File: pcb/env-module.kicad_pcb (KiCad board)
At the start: 4 copper layers, 50 x 30 mm, 68 parts, among them J10 Power Out, J2 QWICC, J5 QWICC, J7 Power In, J9 AVR-UPDI-6, U1 ATtiny1616-MNR, U2 HDC1080, U3 LTR-303ALS-01

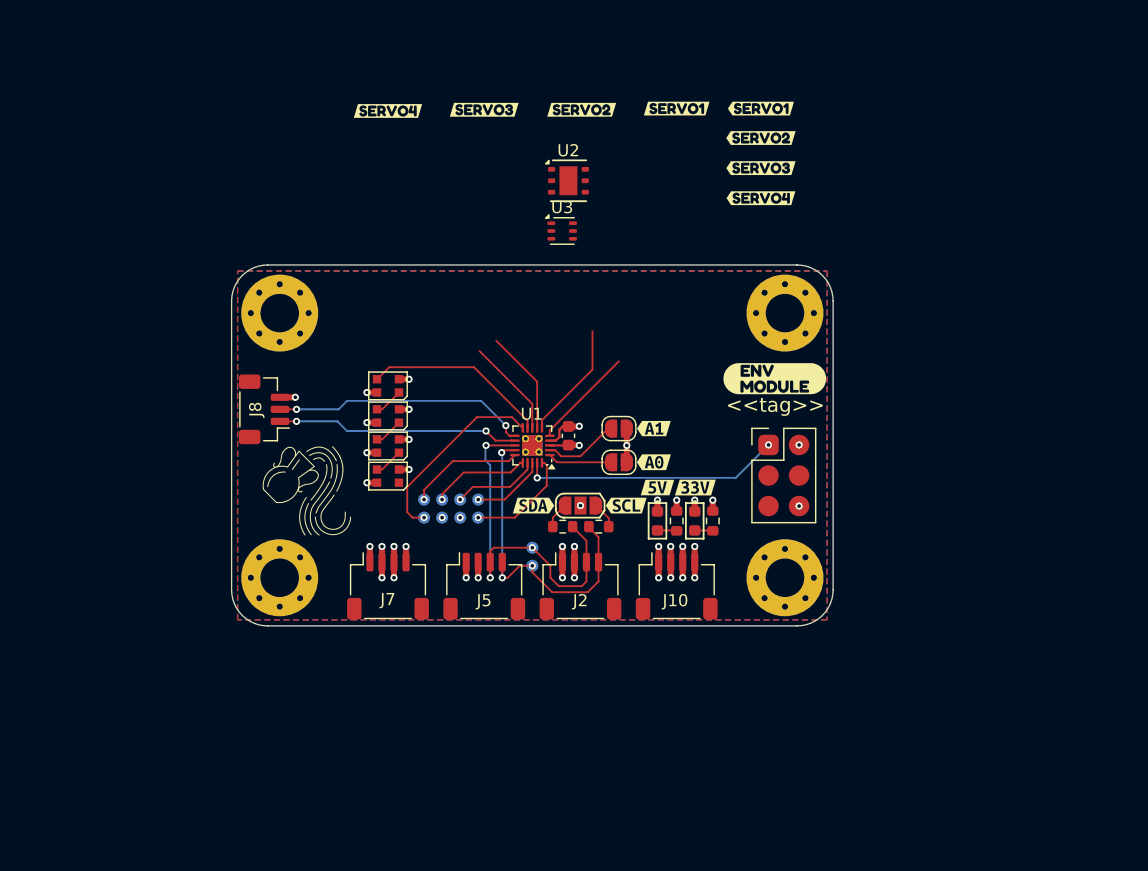
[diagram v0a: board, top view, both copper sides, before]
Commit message: Updated license and implemented RP2040
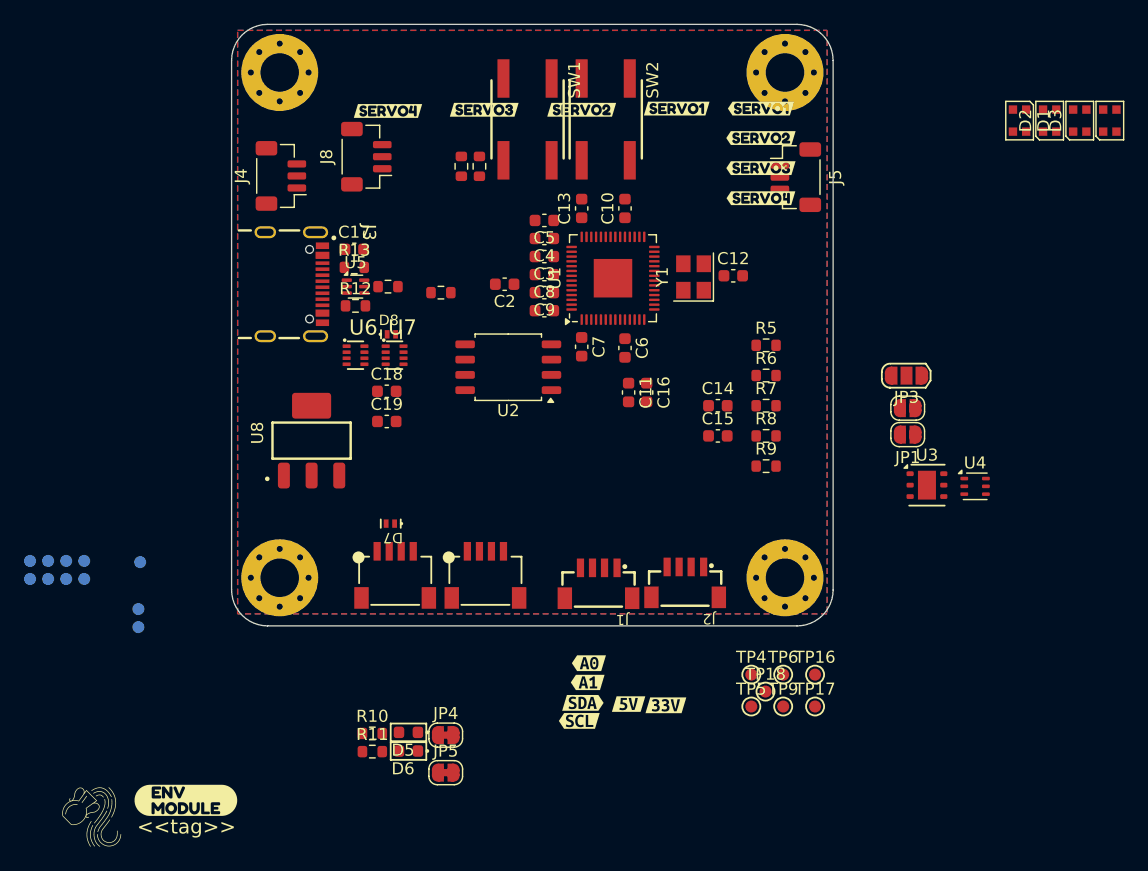
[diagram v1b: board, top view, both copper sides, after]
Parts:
- removed J10: Power Out, CRGM Connector:JST_SH_SM04B-SRSS-TB_1x04-1MP_P1.00mm_Horizontal
- removed J9: AVR-UPDI-6, CRGM Connector:PinHeader_2x03_P2.54mm_Vertical_SMD
- added C10: 0.1uF, Capacitor_SMD:C_0603_1608Metric, F.Cu at (82.7, 75.3)
- added C11: 0.1uF, Capacitor_SMD:C_0603_1608Metric, F.Cu at (83.0, 90.6)
- added C12: 0.1uF, Capacitor_SMD:C_0603_1608Metric, F.Cu at (91.7, 80.9)
- added C13: 0.1uF, Capacitor_SMD:C_0603_1608Metric, F.Cu at (79.1, 75.3)
- added C14: 15pF, Capacitor_SMD:C_0603_1608Metric, F.Cu at (90.4, 91.7)
- added C15: 15pF, Capacitor_SMD:C_0603_1608Metric, F.Cu at (90.4, 94.2)
- added C16: 10uF, Capacitor_SMD:C_0603_1608Metric, F.Cu at (84.5, 90.6)
- added C17: 0.1uF, Capacitor_SMD:C_0603_1608Metric, F.Cu at (60.2, 78.7)
- added C18: 0.1uF, Capacitor_SMD:C_0603_1608Metric, F.Cu at (62.9, 90.5)
- added C19: 10uF, Capacitor_SMD:C_0603_1608Metric, F.Cu at (62.9, 93.0)
- added C2: 0.1uF, Capacitor_SMD:C_0603_1608Metric, F.Cu at (72.7, 81.6)
- added C3: 1uF, Capacitor_SMD:C_0603_1608Metric, F.Cu at (76.0, 79.3)
- added C4: 1uF, Capacitor_SMD:C_0603_1608Metric, F.Cu at (76.0, 77.8)
- added C5: 0.1uF, Capacitor_SMD:C_0603_1608Metric, F.Cu at (76.0, 76.3)
- added C6: 0.1uF, Capacitor_SMD:C_0603_1608Metric, F.Cu at (82.7, 86.9)
- added C7: 0.1uF, Capacitor_SMD:C_0603_1608Metric, F.Cu at (79.1, 86.8)
- added C8: 0.1uF, Capacitor_SMD:C_0603_1608Metric, F.Cu at (76.0, 80.8)
- added C9: 0.1uF, Capacitor_SMD:C_0603_1608Metric, F.Cu at (76.0, 82.3)
- added D1: WS2812B-2020, LED_SMD:LED_WS2812B-2020_PLCC4_2.0x2.0mm, F.Cu at (115.5, 68.0)
- added D8: PESD3V3S1BL, CRGM Passive:DFN1006-2, F.Cu at (63.3, 85.8)
- added J1: ~, CRGM Connector:BM04B-SRSS-TB, F.Cu at (80.5, 105.2)
- added J3: USB_C_USB2.0_16P, CRGM Connector:GCT_USB4105-GF-A, F.Cu at (52.8, 81.6)
- added J4: ~, Connector_JST:JST_SH_BM03B-SRSS-TB_1x03-1MP_P1.00mm_Vertical, F.Cu at (54.1, 72.6)
- added J6: ~, CRGM Connector:SM04B-SRSS-TB, F.Cu at (71.1, 103.8)
- added JP4: ~, CRGM Connector:SolderJumper-2_P1.3mm_Bridged_RoundedPad1.0x1.5mm, F.Cu at (67.8, 119.1)
- added JP5: ~, CRGM Connector:SolderJumper-2_P1.3mm_Bridged_RoundedPad1.0x1.5mm, F.Cu at (67.8, 122.2)
- added R10: 4.7K, Resistor_SMD:R_0603_1608Metric, F.Cu at (61.7, 118.9)
- added R11: 1K, Resistor_SMD:R_0603_1608Metric, F.Cu at (61.7, 120.5)
- added R12: 5.1K, Resistor_SMD:R_0603_1608Metric, F.Cu at (60.3, 83.4)
- added R13: 5.1K, Resistor_SMD:R_0603_1608Metric, F.Cu at (60.2, 80.2)
- added R5: 4.7K, Resistor_SMD:R_0603_1608Metric, F.Cu at (94.4, 86.7)
- added R6: 4.7K, Resistor_SMD:R_0603_1608Metric, F.Cu at (94.4, 89.2)
- added R7: 1K, Resistor_SMD:R_0603_1608Metric, F.Cu at (94.4, 91.7)
- added R8: 4.7K, Resistor_SMD:R_0603_1608Metric, F.Cu at (94.4, 94.2)
- added R9: 4.7K, Resistor_SMD:R_0603_1608Metric, F.Cu at (94.4, 96.7)
- added SW1: EVQ-Q2B02W, CRGM Switches:EVQ-Q2B02W, F.Cu at (74.6, 67.9)
- added SW2: EVQ-Q2B02W, CRGM Switches:EVQ-Q2B02W, F.Cu at (81.1, 67.9)
- added TP16: ~, CRGM Mechanical:TestPoint_Pad_D1.0mm, F.Cu at (98.5, 114.0)
- added TP17: ~, CRGM Mechanical:TestPoint_Pad_D1.0mm, F.Cu at (98.5, 116.7)
- added TP18: ~, CRGM Mechanical:TestPoint_Pad_D1.0mm, F.Cu at (94.4, 115.5)
- added TP4: ~, CRGM Mechanical:TestPoint_Pad_D1.0mm, F.Cu at (93.2, 114.0)
- added TP5: ~, CRGM Mechanical:TestPoint_Pad_D1.0mm, F.Cu at (93.2, 116.7)
- added TP6: ~, CRGM Mechanical:TestPoint_Pad_D1.0mm, F.Cu at (95.8, 114.0)
- added TP9: ~, CRGM Mechanical:TestPoint_Pad_D1.0mm, F.Cu at (95.8, 116.7)
- added U4: LTR-303ALS-01, CRG Makes:LTR-303ALS-01, F.Cu at (111.8, 98.4)
- added U5: USBLC6-2P6, Package_TO_SOT_SMD:SOT-666, F.Cu at (60.3, 81.8)
- added U6: LM66200DRLR, CRGM Power:SOTFL50P160X60-8N, F.Cu at (60.3, 87.5)
- added U7: LM66200DRLR, CRGM Power:SOTFL50P160X60-8N, F.Cu at (63.5, 87.5)
- added U8: LD1117S33TR, CRGM Power:SOT230P700X180-4N, F.Cu at (56.6, 94.6)
- added Y1: ABM8-272-T3, CRGM Passive:Crystal_SMD_3225-4Pin_3.2x2.5mm, F.Cu at (88.4, 81.0)
- D2: value Orange -> WS2812B-2020; footprint LED_SMD:LED_0603_1608Metric -> LED_SMD:LED_WS2812B-2020_PLCC4_2.0x2.0mm
- D3: value Blue -> WS2812B-2020; footprint LED_SMD:LED_0603_1608Metric -> LED_SMD:LED_WS2812B-2020_PLCC4_2.0x2.0mm
- D5, D6: value WS2812B-2020 -> Orange; footprint LED_SMD:LED_WS2812B-2020_PLCC4_2.0x2.0mm -> LED_SMD:LED_0603_1608Metric
- D7: value WS2812B-2020 -> PESD5V5C1BL; footprint LED_SMD:LED_WS2812B-2020_PLCC4_2.0x2.0mm -> CRGM Passive:DFN1006-2
- J2: value QWICC -> ~; footprint CRGM Connector:JST_SH_SM04B-SRSS-TB_1x04-1MP_P1.00mm_Horizontal -> CRGM Connector:BM04B-SRSS-TB
- J5: value QWICC -> ~; footprint CRGM Connector:JST_SH_SM04B-SRSS-TB_1x04-1MP_P1.00mm_Horizontal -> Connector_JST:JST_SH_BM03B-SRSS-TB_1x03-1MP_P1.00mm_Vertical
- J7: value Power In -> ~; footprint CRGM Connector:JST_SH_SM04B-SRSS-TB_1x04-1MP_P1.00mm_Horizontal -> CRGM Connector:SM04B-SRSS-TB
- J8: value ~ -> BM03B-SRSS-TB; footprint CRGM Connector:JST_SH_BM03B-SRSS-TB_1x03-1MP_P1.00mm_Vertical -> Connector_JST:JST_SH_BM03B-SRSS-TB_1x03-1MP_P1.00mm_Vertical
- JP1: value Jumper_3_Open -> ~; footprint CRGM Connector:SolderJumper-3_P1.3mm_Open_RoundedPad1.0x1.5mm -> CRGM Connector:SolderJumper-2_P1.3mm_Open_RoundedPad1.0x1.5mm
- JP2: value A0 -> ~
- JP3: value A1 -> Jumper_3_Open; footprint CRGM Connector:SolderJumper-2_P1.3mm_Open_RoundedPad1.0x1.5mm -> CRGM Connector:SolderJumper-3_P1.3mm_Open_RoundedPad1.0x1.5mm
- LOGO1: footprint CRGM Logos:Aquarius Logo 8mm -> CRGM Logos:CRGM Logo 10mm
- LOGO2: footprint CRGM Logos:Aquarius Logo 8mm -> CRGM Logos:Aquarius Logo 5mm
- LOGO3: value Logo_Open_Hardware_Small -> ~; footprint Symbol:OSHW-Logo_5.7x6mm_SilkScreen -> CRGM Logos:Aquarius Logo 5mm
- LOGO4: value ~ -> Logo_Open_Hardware_Small; footprint CRGM Logos:CRGM Logo 5mm -> Symbol:OSHW-Logo_5.7x6mm_SilkScreen
- R1: value 4.7K -> 10K
- R2: value 4.7K -> 1K
- R3: value 4.7K -> 27
- R4: value 1K -> 27
- TP1: value PA1 -> ~
- TP10: value UPDI -> ~
- TP11: value V33 -> ~
- TP12: value GND -> ~
- TP13: value PB3 -> ~
- TP14: value PC3 -> ~
- TP15: value PC2 -> ~
- TP2: value PC0 -> ~
- TP3: value PC1 -> ~
- TP7: value SCL -> ~
- TP8: value SDA -> ~
- U1: value ATtiny1616-MNR -> RP2040; footprint CRG Makes:VQFN-20-1EP_3x3mm_P0.4mm_EP1.7x1.7mm_ThermalVias -> Package_DFN_QFN:QFN-56-1EP_7x7mm_P0.4mm_EP3.2x3.2mm
- U2: value HDC1080 -> W25Q128JVS; footprint CRG Makes:PWSON-N6 -> CRG Makes:SOIC-8_5.3x5.3mm_P1.27mm
- U3: value LTR-303ALS-01 -> HDC1080; footprint CRG Makes:LTR-303ALS-01 -> CRG Makes:PWSON-N6
- moved D4 63.9 mm to (123.0, 68.0), turned to 90 degrees
- moved kibuzzard-68645E77 60.2 mm to (46.2, 124.5)
- moved TP10 53.1 mm to (42.4, 104.7)
- moved D2 46.6 mm to (118.0, 68.0), turned to 90 degrees
- moved D3 46.2 mm to (120.5, 68.0), turned to 90 degrees
- moved J5 42.7 mm to (96.9, 72.7), turned to -90 degrees
- moved LOGO1 42.7 mm to (82.4, 132.3)
- moved kibuzzard-68586251 42.6 mm to (25.8, 111.0)
- moved kibuzzard-6861B7EA 42.6 mm to (28.8, 111.0)
- moved kibuzzard-6861B80B 42.6 mm to (30.2, 111.0)
- moved kibuzzard-6861B833 42.6 mm to (27.3, 111.0)
- moved kibuzzard-68645E60 42.2 mm to (63.5, 126.0)
- moved kibuzzard-6861B880 41.9 mm to (27.2, 114.9)
- moved kibuzzard-6861B899 41.9 mm to (25.7, 114.9)
- moved kibuzzard-6862CEAB 41.9 mm to (30.2, 114.9)
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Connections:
- net SERVO1 renamed MOSI
- net SERVO2 renamed MISO
- net SERVO4 renamed SCK
- C1 pad 1: +3.3V -> +1V1
- D2 pad 1: GND -> Net-(D2-DOUT)
- D2 pad 2: /Indicators/V5LED -> GND
- D3 pad 1: GND -> Net-(D3-DOUT)
- D3 pad 2: /Indicators/V3.3LED -> GND
- D4 pad 1: Net-(D4-DOUT) -> unconnected-(D4-DOUT-Pad1)
- D4 pad 3: STATUS_LEDS -> Net-(D3-DOUT)
- D5 pad 1: Net-(D5-DOUT) -> Net-(D5-K)
- D5 pad 2: GND -> /Indicators/V5LED
- D6 pad 1: Net-(D6-DOUT) -> Net-(D6-K)
- D6 pad 2: GND -> /Indicators/V3.3LED
- D7 pad 1: unconnected-(D7-DOUT-Pad1) -> GND
- D7 pad 2: GND -> LINE_5V
- J2 pad 3: SDA -> SDA_EXT
- J2 pad 4: SCL -> SCL_EXT
- J5 pad 1: GND -> SWCLK
- J5 pad 2: +3.3V -> GND
- J5 pad 3: SDA -> SWD
- J7 pad 1: +5V -> LINE_5V
- J7 pad 4: +3.3V -> LINE_V33
- J8 pad 1: TXD -> GND
- J8 pad 2: RXD -> +3.3V
- J8 pad 3: GND -> EXT_LEDS
- JP1 pad 1: Net-(JP1-A) -> GND
- JP1 pad 2: +3.3V -> /MCU/A1
- JP3 pad 1: GND -> Net-(JP3-A)
- JP3 pad 2: /MCU/A1 -> +3.3V
- R1 pad 1: SDA -> +3.3V
- R1 pad 2: Net-(JP1-B) -> /MCU/QSPI_CS
- R2 pad 1: SCL -> USBBOOT
- R2 pad 2: Net-(JP1-A) -> /MCU/QSPI_CS
- R3 pad 1: +5V -> Net-(U1-USB_DP)
- R3 pad 2: /Indicators/V5LED -> D_P
- R4 pad 1: +3.3V -> Net-(U1-USB_DM)
- R4 pad 2: /Indicators/V3.3LED -> D_N
- TP1 pad 1: /MCU/PA1 -> USB_5V
- TP10 pad 1: UPDI -> SWCLK
- TP11 pad 1: +3.3V -> SWD
- TP12 pad 1: GND -> LINE_V33
- TP13 pad 1: /MCU/PB4 -> LINE_5V
- TP14 pad 1: /MCU/PC3 -> EXT_LEDS
- TP15 pad 1: /MCU/PC2 -> +5V
- TP2 pad 1: /MCU/PC0 -> SCL_EXT
- TP3 pad 1: /MCU/PC1 -> SDA_EXT
- TP7 pad 1: SCL -> D_P
- TP8 pad 1: SDA -> TXD
- U1 pad 1: /MCU/A0 -> +3.3V
- U1 pad 10: /MCU/PB4 -> +3.3V
- U1 pad 11: RXD -> EXT_LEDS
- U1 pad 12: TXD -> unconnected-(U1-GPIO9-Pad12)
- U1 pad 13: SDA -> unconnected-(U1-GPIO10-Pad13)
- U1 pad 14: SCL -> unconnected-(U1-GPIO11-Pad14)
- U1 pad 15: /MCU/PC0 -> unconnected-(U1-GPIO12-Pad15)
- U1 pad 16: /MCU/PC1 -> unconnected-(U1-GPIO13-Pad16)
- U1 pad 17: /MCU/PC2 -> unconnected-(U1-GPIO14-Pad17)
- U1 pad 18: /MCU/PC3 -> unconnected-(U1-GPIO15-Pad18)
- U1 pad 19: UPDI -> GND
- U1 pad 2: /MCU/A1 -> /MCU/A0
- U1 pad 20: /MCU/PA1 -> Net-(U1-XIN)
- U1 pad 21: GND -> Net-(U1-XOUT)
- U1 pad 3: GND -> /MCU/A1
- U1 pad 4: +3.3V -> unconnected-(U1-GPIO2-Pad4)
- U1 pad 7: SERVO3 -> RXD
- U1 pad 9: STATUS_LEDS -> OBLEDS
- U2 pad 1: unconnected-(U2-SDA-Pad1) -> /MCU/QSPI_CS
- U2 pad 2: unconnected-(U2-GND-Pad2) -> /MCU/QSPI_D1
- U2 pad 3: unconnected-(U2-NC-Pad3) -> /MCU/QSPI_D2
- U2 pad 4: unconnected-(U2-NC-Pad4) -> GND
- U2 pad 5: unconnected-(U2-VCC-Pad5) -> /MCU/QSPI_D0
- U2 pad 6: unconnected-(U2-SCL-Pad6) -> /MCU/QSPI_SCK
- U2 pad 7: unconnected-(U2-DAP-Pad7) -> /MCU/QSPI_D3
- U3 pad 1: unconnected-(U3-VDD-Pad1) -> SDA_INT
- U3 pad 2: unconnected-(U3-NC-Pad2) -> GND
- U3 pad 5: unconnected-(U3-INT-Pad5) -> +3.3V
- U3 pad 6: unconnected-(U3-SDA-Pad6) -> SCL_INT
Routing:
- net SDA: track 31.0 -> 0.00 mm, vias 3 -> 0
- net SCL: track 27.8 -> 0.00 mm, vias 3 -> 0
- net GND: track 26.1 -> 0.00 mm, vias 22 -> 0
- net UPDI: track 21.6 -> 0.00 mm, vias 2 -> 0
- net RXD: track 21.3 -> 0.00 mm, vias 2 -> 0
- net TXD: track 20.2 -> 0.00 mm, vias 2 -> 0
- net /MCU/PB4: track 16.3 -> 0.00 mm, vias 1 -> 0
- net STATUS_LEDS: track 15.4 -> 0.00 mm
- net +3.3V: track 15.3 -> 0.00 mm, vias 15 -> 0
- net MISO: track 9.79 -> 0.00 mm
- net /MCU/PC0: track 9.55 -> 0.00 mm, vias 1 -> 0
- net /MCU/PA1: track 8.98 -> 0.00 mm, vias 1 -> 0
- net SERVO3: track 8.66 -> 0.00 mm
- net MOSI: track 8.58 -> 0.00 mm
- net /MCU/PC1: track 8.23 -> 0.00 mm, vias 1 -> 0
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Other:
- board size 50 x 30 mm -> 50 x 50 mm

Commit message: Added interfaces and fully routed PCB
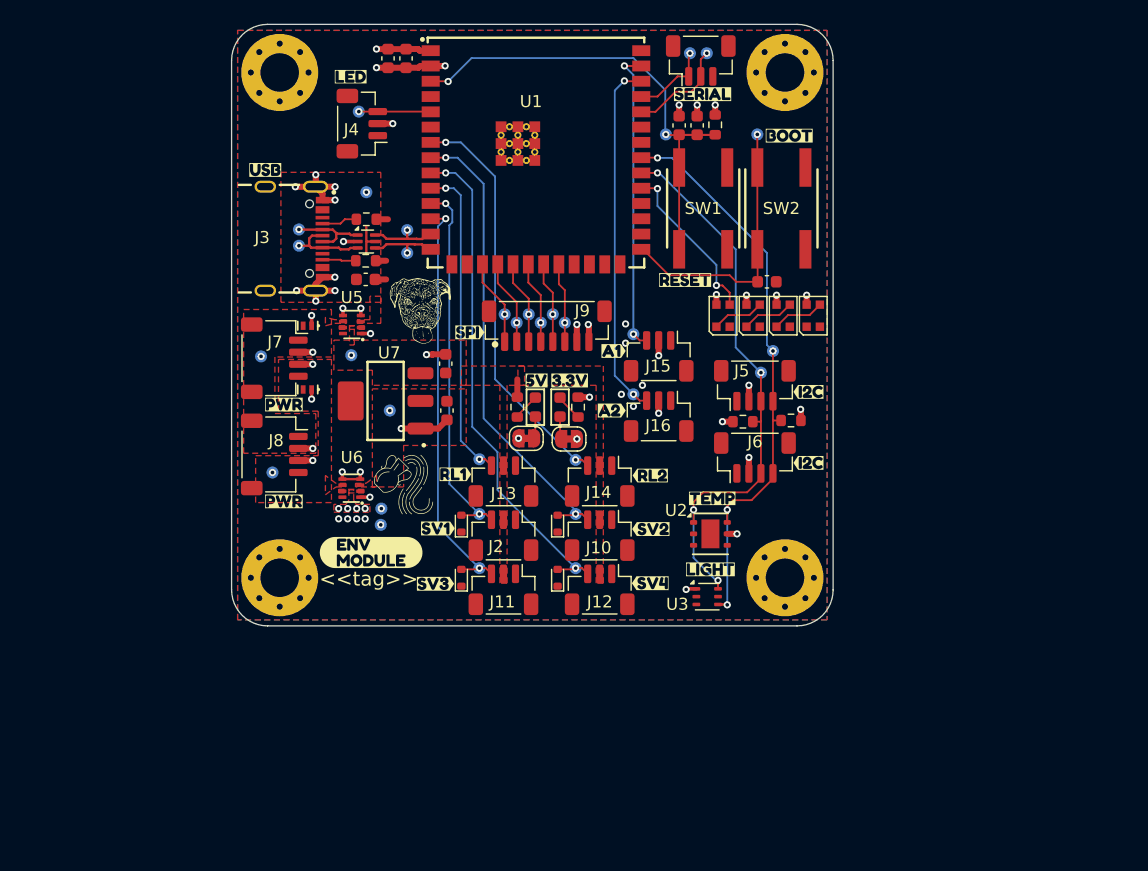
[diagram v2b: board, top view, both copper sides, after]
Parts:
- removed C10, C11, C12, C13, C17, C18, C9: 0.1uF, Capacitor_SMD:C_0603_1608Metric
- removed C14, C15: 15pF, Capacitor_SMD:C_0603_1608Metric
- removed C16, C19: 10uF, Capacitor_SMD:C_0603_1608Metric
- removed JP1: ~, CRGM Connector:SolderJumper-2_P1.3mm_Open_RoundedPad1.0x1.5mm
- removed JP4, JP5: ~, CRGM Connector:SolderJumper-2_P1.3mm_Bridged_RoundedPad1.0x1.5mm
- removed R10, R6: 4.7K, Resistor_SMD:R_0603_1608Metric
- removed R11, R7: 1K, Resistor_SMD:R_0603_1608Metric
- removed R12, R13: 5.1K, Resistor_SMD:R_0603_1608Metric
- removed TP1: ~, CRGM Mechanical:TestPoint_Pad_D1.0mm
- removed U8: LD1117S33TR, CRGM Power:SOT230P700X180-4N
- removed Y1: ABM8-272-T3, CRGM Passive:Crystal_SMD_3225-4Pin_3.2x2.5mm
- removed kibuzzard-68583EA9: G***, kibuzzard-68583EA9
- removed kibuzzard-68583EC3: G***, kibuzzard-68583EC3
- removed kibuzzard-68583EE4: G***, kibuzzard-68583EE4
- removed kibuzzard-68583EEB: G***, kibuzzard-68583EEB
- removed kibuzzard-68583F01: G***, kibuzzard-68583F01
- removed kibuzzard-68583F18: G***, kibuzzard-68583F18
- removed kibuzzard-68583F22: G***, kibuzzard-68583F22
- removed kibuzzard-68583F28: G***, kibuzzard-68583F28
- removed kibuzzard-6858441E: G***, kibuzzard-6858441E
- removed kibuzzard-6858446E: G***, kibuzzard-6858446E
- removed kibuzzard-68584599: G***, kibuzzard-68584599
- removed kibuzzard-685845A0: G***, kibuzzard-685845A0
- removed kibuzzard-685845CF: G***, kibuzzard-685845CF
- removed kibuzzard-685845E1: G***, kibuzzard-685845E1
- removed kibuzzard-68586251: G***, kibuzzard-68586251
- removed kibuzzard-6861B7EA: G***, kibuzzard-6861B7EA
- removed kibuzzard-6861B80B: G***, kibuzzard-6861B80B
- removed kibuzzard-6861B833: G***, kibuzzard-6861B833
- removed kibuzzard-6861B880: G***, kibuzzard-6861B880
- removed kibuzzard-6861B899: G***, kibuzzard-6861B899
- removed kibuzzard-6862CEAB: G***, kibuzzard-6862CEAB
- removed kibuzzard-6862CEB9: G***, kibuzzard-6862CEB9
- removed kibuzzard-6862CEC0: G***, kibuzzard-6862CEC0
- removed kibuzzard-6862CEE4: G***, kibuzzard-6862CEE4
- added D10: PESD5V0S1BB, CRGM Passive:D_SOD-523, F.Cu at (77.1, 101.5)
- added D11: PESD5V0S1BB, CRGM Passive:D_SOD-523, F.Cu at (69.1, 106.0)
- added D12: PESD5V0S1BB, CRGM Passive:D_SOD-523, F.Cu at (77.1, 106.0)
- added D9: PESD5V0S1BB, CRGM Passive:D_SOD-523, F.Cu at (69.1, 101.5)
- added J10: ~, CRGM Connector:JST_SH_BM03B-SRSS-TB_1x03-1MP_P1.00mm_Vertical, F.Cu at (80.6, 102.5)
- added J11: ~, CRGM Connector:JST_SH_BM03B-SRSS-TB_1x03-1MP_P1.00mm_Vertical, F.Cu at (72.6, 107.0)
- added J12: ~, CRGM Connector:JST_SH_BM03B-SRSS-TB_1x03-1MP_P1.00mm_Vertical, F.Cu at (80.6, 107.0)
- added J13: ~, CRGM Connector:JST_SH_BM03B-SRSS-TB_1x03-1MP_P1.00mm_Vertical, F.Cu at (72.6, 98.0)
- added J14: ~, CRGM Connector:JST_SH_BM03B-SRSS-TB_1x03-1MP_P1.00mm_Vertical, F.Cu at (80.6, 98.0)
- added J15: ~, CRGM Connector:JST_SH_BM03B-SRSS-TB_1x03-1MP_P1.00mm_Vertical, F.Cu at (85.5, 87.6)
- added J16: ~, CRGM Connector:JST_SH_BM03B-SRSS-TB_1x03-1MP_P1.00mm_Vertical, F.Cu at (85.5, 92.6)
- added J9: BM08B-SRSS-TB, CRGM Connector:JST_SH_BM08B-SRSS-TB_1x08-1MP_P1.00mm_Vertical, F.Cu at (76.2, 85.0)
- added TP19: ~, CRGM Mechanical:TestPoint_Pad_D1.0mm, B.Cu at (76.7, 84.1)
- added TP20: ~, CRGM Mechanical:TestPoint_Pad_D1.0mm, B.Cu at (77.7, 84.8)
- added TP21: ~, CRGM Mechanical:TestPoint_Pad_D1.0mm, B.Cu at (52.5, 87.6)
- added TP22: ~, CRGM Mechanical:TestPoint_Pad_D1.0mm, B.Cu at (60.0, 87.5)
- added TP23: ~, CRGM Mechanical:TestPoint_Pad_D1.0mm, B.Cu at (62.5, 100.2)
- added TP24: ~, CRGM Mechanical:TestPoint_Pad_D1.0mm, B.Cu at (62.4, 101.6)
- added TP25: ~, CRGM Mechanical:TestPoint_Pad_D1.0mm, B.Cu at (63.1, 92.1)
- added TP26: ~, CRGM Mechanical:TestPoint_Pad_D1.0mm, B.Cu at (70.6, 100.7)
- added TP27: ~, CRGM Mechanical:TestPoint_Pad_D1.0mm, B.Cu at (78.6, 100.7)
- added TP28: ~, CRGM Mechanical:TestPoint_Pad_D1.0mm, B.Cu at (70.6, 105.2)
- added TP29: ~, CRGM Mechanical:TestPoint_Pad_D1.0mm, B.Cu at (78.6, 105.2)
- added TP30: ~, CRGM Mechanical:TestPoint_Pad_D1.0mm, B.Cu at (70.6, 96.2)
- added TP31: ~, CRGM Mechanical:TestPoint_Pad_D1.0mm, B.Cu at (78.6, 96.2)
- added TP32: ~, CRGM Mechanical:TestPoint_Pad_D1.0mm, B.Cu at (83.4, 85.8)
- added TP33: ~, CRGM Mechanical:TestPoint_Pad_D1.0mm, B.Cu at (83.4, 90.8)
- added kibuzzard-6812E37E: G***, kibuzzard-6812E37E, B.Cu at (73.7, 86.0)
- added kibuzzard-6812E3A0: G***, kibuzzard-6812E3A0, B.Cu at (74.7, 83.0)
- added kibuzzard-6812E3AD: G***, kibuzzard-6812E3AD, B.Cu at (77.5, 85.9)
- added kibuzzard-6812E3BB: G***, kibuzzard-6812E3BB, B.Cu at (76.7, 83.0)
- added kibuzzard-6812E3C5: G***, kibuzzard-6812E3C5, B.Cu at (75.7, 86.0)
- added kibuzzard-6812E420: G***, kibuzzard-6812E420, B.Cu at (72.7, 83.0)
- added kibuzzard-68194F3F: G***, kibuzzard-68194F3F, B.Cu at (78.7, 85.9)
- added kibuzzard-68194F50: G***, kibuzzard-68194F50, B.Cu at (79.7, 85.9)
- added kibuzzard-68927DC7: G***, kibuzzard-68927DC7, B.Cu at (97.1, 87.2)
- added kibuzzard-68927E23: G***, kibuzzard-68927E23, B.Cu at (74.1, 105.2)
- added kibuzzard-68927E44: G***, kibuzzard-68927E44, B.Cu at (74.0, 100.8)
- added kibuzzard-68927E4C: G***, kibuzzard-68927E4C, B.Cu at (82.2, 100.8)
- added kibuzzard-68927E53: G***, kibuzzard-68927E53, B.Cu at (82.2, 105.2)
- added kibuzzard-68927E88: G***, kibuzzard-68927E88, B.Cu at (62.7, 77.2)
- added kibuzzard-68927E94: G***, kibuzzard-68927E94, B.Cu at (62.8, 79.0)
- added kibuzzard-68927EA7: G***, kibuzzard-68927EA7, B.Cu at (53.2, 77.1)
- added kibuzzard-68927EAF: G***, kibuzzard-68927EAF, B.Cu at (53.2, 78.4)
- added kibuzzard-68927ED6: G***, kibuzzard-68927ED6, B.Cu at (64.3, 74.0)
- added kibuzzard-68927EE6: G***, kibuzzard-68927EE6, B.Cu at (63.8, 67.1)
- added kibuzzard-68927F31: G***, kibuzzard-68927F31, B.Cu at (52.9, 98.7)
- added kibuzzard-68927F82: G***, kibuzzard-68927F82, B.Cu at (59.4, 92.1)
- added kibuzzard-68927FCA: G***, kibuzzard-68927FCA, B.Cu at (96.7, 69.2)
- added kibuzzard-68927FD5: G***, kibuzzard-68927FD5, B.Cu at (84.2, 69.2)
- added kibuzzard-68927FE6: G***, kibuzzard-68927FE6, B.Cu at (91.5, 62.4)
- added kibuzzard-68927FEB: G***, kibuzzard-68927FEB, B.Cu at (86.1, 62.4)
- added kibuzzard-68928016: G***, kibuzzard-68928016, B.Cu at (64.7, 101.7)
- added kibuzzard-68937D96: G***, kibuzzard-68937D96, B.Cu at (96.2, 89.0)
- added kibuzzard-68937DDF: G***, kibuzzard-68937DDF, B.Cu at (82.1, 96.2)
- added kibuzzard-68937DF0: G***, kibuzzard-68937DF0, B.Cu at (74.0, 96.2)
- added kibuzzard-6894D6EB: G***, kibuzzard-6894D6EB, B.Cu at (64.8, 100.2)
- added kibuzzard-6894D76E: G***, kibuzzard-6894D76E, B.Cu at (61.9, 87.5)
- added kibuzzard-6894D783: G***, kibuzzard-6894D783, B.Cu at (54.6, 87.7)
- added kibuzzard-68953BE7: G***, kibuzzard-68953BE7, F.Cu at (89.8, 105.3)
- added kibuzzard-68953C01: G***, kibuzzard-68953C01, F.Cu at (90.0, 99.4)
- added kibuzzard-68953CB6: G***, kibuzzard-68953CB6, F.Cu at (75.3, 89.6)
- added kibuzzard-68953CBF: G***, kibuzzard-68953CBF, F.Cu at (78.1, 89.6)
- added kibuzzard-68953D9F: G***, kibuzzard-68953D9F, F.Cu at (59.9, 64.3)
- added kibuzzard-68953DBA: G***, kibuzzard-68953DBA, F.Cu at (89.2, 65.8)
- added kibuzzard-68953DE5: G***, kibuzzard-68953DE5, F.Cu at (87.7, 81.2)
- added kibuzzard-68953DED: G***, kibuzzard-68953DED, F.Cu at (96.3, 69.2)
- added kibuzzard-68953E3E: G***, kibuzzard-68953E3E, F.Cu at (54.4, 91.6)
- added kibuzzard-68953E3E: G***, kibuzzard-68953E3E, F.Cu at (54.4, 99.7)
- added kibuzzard-68953E7E: G***, kibuzzard-68953E7E, F.Cu at (52.8, 72.1)
- added kibuzzard-68953EC7: G***, kibuzzard-68953EC7, F.Cu at (68.6, 97.4)
- added kibuzzard-68953ED1: G***, kibuzzard-68953ED1, F.Cu at (67.2, 101.9)
- added kibuzzard-68953ED8: G***, kibuzzard-68953ED8, F.Cu at (67.0, 106.5)
- added kibuzzard-68953EE0: G***, kibuzzard-68953EE0, F.Cu at (84.8, 106.5)
- added kibuzzard-68953EEB: G***, kibuzzard-68953EEB, F.Cu at (84.8, 102.0)
- added kibuzzard-68953EF4: G***, kibuzzard-68953EF4, F.Cu at (84.8, 97.5)
- added kibuzzard-68953F10: G***, kibuzzard-68953F10, F.Cu at (69.8, 85.6)
- added kibuzzard-68953F1F: G***, kibuzzard-68953F1F, F.Cu at (98.0, 96.5)
- added kibuzzard-68953F32: G***, kibuzzard-68953F32, F.Cu at (98.0, 90.5)
- added kibuzzard-68953F58: G***, kibuzzard-68953F58, F.Cu at (81.8, 87.2)
- added kibuzzard-68953F6B: G***, kibuzzard-68953F6B, F.Cu at (81.6, 92.1)
- C1: value 0.1uF -> 1uF
- C4: value 1uF -> 0.1uF
- C8: value 0.1uF -> 10uF
- D5: value Orange -> PESD5V5C1BL; footprint LED_SMD:LED_0603_1608Metric -> CRGM Passive:DFN1006-2
- D6: value Orange -> PESD3V3S1BL; footprint LED_SMD:LED_0603_1608Metric -> CRGM Passive:DFN1006-2
- D7: value PESD5V5C1BL -> Orange; footprint CRGM Passive:DFN1006-2 -> LED_SMD:LED_0603_1608Metric
- D8: value PESD3V3S1BL -> Orange; footprint CRGM Passive:DFN1006-2 -> LED_SMD:LED_0603_1608Metric
- H1, H2, H3, H4: value MountingHole -> ~
- J1, J2: footprint CRGM Connector:BM04B-SRSS-TB -> CRGM Connector:JST_SH_BM03B-SRSS-TB_1x03-1MP_P1.00mm_Vertical
- J4: value ~ -> BM03B-SRSS-TB; footprint Connector_JST:JST_SH_BM03B-SRSS-TB_1x03-1MP_P1.00mm_Vertical -> CRGM Connector:JST_SH_BM03B-SRSS-TB_1x03-1MP_P1.00mm_Vertical
- J5: footprint Connector_JST:JST_SH_BM03B-SRSS-TB_1x03-1MP_P1.00mm_Vertical -> CRGM Connector:JST_SH_BM04B-SRSS-TB_1x04-1MP_P1.00mm_Vertical
- J6: footprint CRGM Connector:SM04B-SRSS-TB -> CRGM Connector:JST_SH_BM04B-SRSS-TB_1x04-1MP_P1.00mm_Vertical
- J7: footprint CRGM Connector:SM04B-SRSS-TB -> CRGM Connector:JST_SH_SM04B-SRSS-TB_1x04-1MP_P1.00mm_Horizontal
- J8: value BM03B-SRSS-TB -> ~; footprint Connector_JST:JST_SH_BM03B-SRSS-TB_1x03-1MP_P1.00mm_Vertical -> CRGM Connector:JST_SH_SM04B-SRSS-TB_1x04-1MP_P1.00mm_Horizontal
- JP2: footprint CRGM Connector:SolderJumper-2_P1.3mm_Open_RoundedPad1.0x1.5mm -> CRGM Connector:SolderJumper-2_P1.3mm_Bridged_RoundedPad1.0x1.5mm
- JP3: value Jumper_3_Open -> ~; footprint CRGM Connector:SolderJumper-3_P1.3mm_Open_RoundedPad1.0x1.5mm -> CRGM Connector:SolderJumper-2_P1.3mm_Bridged_RoundedPad1.0x1.5mm
- LOGO1: footprint CRGM Logos:CRGM Logo 10mm -> CRGM Logos:CRGM Logo 5mm
- LOGO4: value Logo_Open_Hardware_Small -> ~
- R2: value 1K -> 4.7K
- R3: value 27 -> 4.7K
- R4: value 27 -> 5.1K
- R5: value 4.7K -> 5.1K
- R9: value 4.7K -> 1K
- TP16, TP17, TP18, TP4, TP5, TP6, TP9: moved to B.Cu
- U1: value RP2040 -> ESP32-S3-WROOM-1-N8R2; footprint Package_DFN_QFN:QFN-56-1EP_7x7mm_P0.4mm_EP3.2x3.2mm -> CRG Makes:ESP32-S3-WROOM-1-N8R2
- U2: value W25Q128JVS -> HDC1080; footprint CRG Makes:SOIC-8_5.3x5.3mm_P1.27mm -> CRG Makes:PWSON-N6
- U3: value HDC1080 -> LTR-303ALS-01; footprint CRG Makes:PWSON-N6 -> CRG Makes:LTR-303ALS-01
- U4: value LTR-303ALS-01 -> USBLC6-2P6; footprint CRG Makes:LTR-303ALS-01 -> Package_TO_SOT_SMD:SOT-666
- U5: value USBLC6-2P6 -> LM66200DRLR; footprint Package_TO_SOT_SMD:SOT-666 -> CRGM Power:SOTFL50P160X60-8N
- U7: value LM66200DRLR -> LD1117S33TR; footprint CRGM Power:SOTFL50P160X60-8N -> CRGM Power:SOT230P700X180-4N
- moved TP2 69.2 mm to (88.1, 62.4), turned to -90 degrees
- moved TP3 69.1 mm to (89.5, 62.4), turned to -90 degrees
- moved TP13 63.1 mm to (94.0, 89.0), turned to 90 degrees
- moved LOGO3 62.3 mm to (78.8, 72.9)
- moved TP12 61.7 mm to (95.0, 87.2), turned to 90 degrees
- moved LOGO1 58.1 mm to (93.6, 75.3)
- moved TP9 56.5 mm to (55.6, 77.0), turned to 180 degrees
- moved U4 54.5 mm to (61.2, 78.0)
- moved TP6 53.0 mm to (61.2, 74.0), turned to 180 degrees
- moved kibuzzard-68645E60 51.8 mm to (76.3, 75.8)
- moved TP5 47.6 mm to (93.7, 69.2), turned to 180 degrees
- moved TP11 46.7 mm to (60.6, 67.2)
- moved TP4 45.5 mm to (86.1, 69.2), turned to 180 degrees
- moved J1 43.0 mm to (89.0, 63.0), turned to 0 degrees
- moved TP15 41.8 mm to (72.7, 84.1)
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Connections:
- C1 pad 1: +1V1 -> +3.3V
- C2 pad 1: +1V1 -> +3.3V
- C3 pad 1: +1V1 -> EN
- C4 pad 1: +3.3V -> EN
- C5 pad 1: +3.3V -> BOOT
- C6 pad 1: +3.3V -> USB_5V
- C7 pad 1: +3.3V -> +5V
- C8 pad 1: +3.3V -> LDO_V33
- D5 pad 1: Net-(D5-K) -> GND
- D5 pad 2: /Indicators/V5LED -> LINE_5V
- D6 pad 1: Net-(D6-K) -> GND
- D6 pad 2: /Indicators/V3.3LED -> LINE_V33
- D7 pad 1: GND -> Net-(D7-K)
- D7 pad 2: LINE_5V -> /Power/V5LED
- D8 pad 1: GND -> Net-(D8-K)
- D8 pad 2: LINE_V33 -> /Power/V3.3LED
- J1 pad 1: GND -> TXD
- J1 pad 2: +3.3V -> RXD
- J1 pad 3: SDA_EXT -> GND
- J2 pad 2: +3.3V -> +5V
- J2 pad 3: SDA_EXT -> SERVO1
- J3 pad A5: /Interfaces/CC1 -> /MCU/CC1
- J3 pad B5: /Interfaces/CC2 -> /MCU/CC2
- J4 pad 1: TXD -> GND
- J4 pad 2: RXD -> +3.3V
- J4 pad 3: GND -> EXT_LEDS
- J5 pad 1: SWCLK -> GND
- J5 pad 2: GND -> +3.3V
- J5 pad 3: SWD -> SDA
- J6 pad 1: LINE_5V -> GND
- J6 pad 2: GND -> +3.3V
- J6 pad 3: GND -> SDA
- J6 pad 4: LINE_V33 -> SCL
- J8 pad 1: GND -> LINE_5V
- J8 pad 2: +3.3V -> GND
- J8 pad 3: EXT_LEDS -> GND
- JP2 pad 2: /MCU/A0 -> Net-(D7-K)
- JP3 pad 1: Net-(JP3-A) -> GND
- JP3 pad 2: +3.3V -> Net-(D8-K)
- R1 pad 2: /MCU/QSPI_CS -> EN
- R2 pad 1: USBBOOT -> SCL
- R2 pad 2: /MCU/QSPI_CS -> +3.3V
- R3 pad 1: Net-(U1-USB_DP) -> SDA
- R3 pad 2: D_P -> +3.3V
- R4 pad 1: Net-(U1-USB_DM) -> /MCU/CC2
- R4 pad 2: D_N -> GND
- R5 pad 1: SCL_INT -> /MCU/CC1
- R5 pad 2: +3.3V -> GND
- R8 pad 1: SDA_EXT -> +5V
- R8 pad 2: Net-(JP3-B) -> /Power/V5LED
- R9 pad 1: SCL_EXT -> +3.3V
- R9 pad 2: Net-(JP3-A) -> /Power/V3.3LED
- SW1 pad B1: USBBOOT -> EN
- SW1 pad B2: USBBOOT -> EN
- SW2 pad B1: RUN -> BOOT
- SW2 pad B2: RUN -> BOOT
- TP10 pad 1: SWCLK -> USB_D_P
- TP11 pad 1: SWD -> EXT_LEDS
- TP12 pad 1: LINE_V33 -> SCL
- TP13 pad 1: LINE_5V -> SDA
- TP14 pad 1: EXT_LEDS -> LINE_V33
- TP15 pad 1: +5V -> SPI_IRQ0
- TP16 pad 1: +3.3V -> SPI_CE0
- TP17 pad 1: GND -> SPI_CS0
- TP18 pad 1: LDO_V33 -> SPI_MISO
- TP2 pad 1: SCL_EXT -> TXD
- TP3 pad 1: SDA_EXT -> RXD
- TP4 pad 1: USB_D_N -> EN
- TP5 pad 1: USB_D_P -> BOOT
- TP6 pad 1: D_N -> USB_5V
- TP7 pad 1: D_P -> D_N
- TP8 pad 1: TXD -> D_P
- TP9 pad 1: RXD -> USB_D_N
- U1 pad 1: +3.3V -> GND
- U1 pad 10: +3.3V -> RELAY1
- U1 pad 11: EXT_LEDS -> SERVO1
- U1 pad 12: unconnected-(U1-GPIO9-Pad12) -> SERVO3
- U1 pad 13: unconnected-(U1-GPIO10-Pad13) -> D_N
- U1 pad 14: unconnected-(U1-GPIO11-Pad14) -> D_P
- U1 pad 17: unconnected-(U1-GPIO14-Pad17) -> SPI_IRQ0
- U1 pad 18: unconnected-(U1-GPIO15-Pad18) -> SPI_CE0
- U1 pad 19: GND -> SPI_CS0
- U1 pad 2: /MCU/A0 -> +3.3V
- U1 pad 20: Net-(U1-XIN) -> SPI_MISO
- U1 pad 21: Net-(U1-XOUT) -> SPI_CLK
- U1 pad 22: +3.3V -> SPI_MOSI
- U1 pad 23: +1V1 -> unconnected-(U1-IO21-Pad23)
- U1 pad 24: SWCLK -> unconnected-(U1-IO47-Pad24)
- U1 pad 25: SWD -> unconnected-(U1-IO48-Pad25)
- U1 pad 26: RUN -> unconnected-(U1-IO45-Pad26)
- U1 pad 27: unconnected-(U1-GPIO16-Pad27) -> BOOT
- U1 pad 3: /MCU/A1 -> EN
- U1 pad 31: TXD -> OBLEDS
- U1 pad 32: unconnected-(U1-GPIO21-Pad32) -> SDA
- U1 pad 33: +3.3V -> SCL
- U1 pad 34: SDA_INT -> unconnected-(U1-IO41-Pad34)
- U1 pad 35: SCL_INT -> unconnected-(U1-IO42-Pad35)
- U1 pad 36: SDA_EXT -> RXD
- U1 pad 37: SCL_EXT -> TXD
- U1 pad 38: unconnected-(U1-GPIO26_ADC0-Pad38) -> ADC2
- U1 pad 39: unconnected-(U1-GPIO27_ADC1-Pad39) -> ADC1
- U1 pad 40: unconnected-(U1-GPIO28_ADC2-Pad40) -> GND
- U1 pad 41: unconnected-(U1-GPIO29_ADC3-Pad41) -> GND
- U1 pad 5: MOSI -> EXT_LEDS
- U1 pad 6: MISO -> unconnected-(U1-IO6-Pad6)
- U1 pad 7: RXD -> RELAY2
- U1 pad 8: SCK -> SERVO2
- U1 pad 9: OBLEDS -> SERVO4
- U2 pad 1: /MCU/QSPI_CS -> SDA
- U2 pad 2: /MCU/QSPI_D1 -> GND
- U2 pad 3: /MCU/QSPI_D2 -> unconnected-(U2-NC-Pad3)
- U2 pad 4: GND -> unconnected-(U2-NC-Pad4)
- U2 pad 5: /MCU/QSPI_D0 -> +3.3V
- U2 pad 6: /MCU/QSPI_SCK -> SCL
- U2 pad 7: /MCU/QSPI_D3 -> unconnected-(U2-DAP-Pad7)
- U3 pad 1: SDA_INT -> +3.3V
- U3 pad 2: GND -> unconnected-(U3-NC-Pad2)
- U3 pad 3: unconnected-(U3-NC-Pad3) -> GND
- U3 pad 4: unconnected-(U3-NC-Pad4) -> SCL
- U3 pad 5: +3.3V -> unconnected-(U3-INT-Pad5)
- U3 pad 6: SCL_INT -> SDA
- U4 pad 1: +3.3V -> USB_D_N
- U4 pad 2: unconnected-(U4-NC-Pad2) -> GND
- U4 pad 3: GND -> USB_D_P
- U4 pad 4: SCL_INT -> D_P
- U4 pad 5: unconnected-(U4-INT-Pad5) -> USB_5V
- U4 pad 6: SDA_INT -> D_N
- U5 pad 1: USB_D_N -> GND
- U5 pad 2: GND -> +5V
- U5 pad 3: USB_D_P -> USB_5V
- U5 pad 4: D_P -> GND
- U5 pad 5: USB_5V -> GND
- U5 pad 6: D_N -> LINE_5V
- U6 pad 2: +5V -> +3.3V
- U6 pad 3: USB_5V -> LDO_V33
- U6 pad 6: LINE_5V -> LINE_V33
- U6 pad 7: +5V -> +3.3V
- U7 pad 2: +3.3V -> LDO_V33
- U7 pad 3: LDO_V33 -> +5V
- U7 pad 4: GND -> (no net)
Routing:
- net SCL: track 0.00 -> 49.0 mm, vias 0 -> 4
- net SDA: track 0.00 -> 46.9 mm, vias 0 -> 4
- net GND: track 0.00 -> 42.6 mm, vias 0 -> 39
- net EN: track 0.00 -> 41.8 mm, vias 0 -> 2
- net SERVO4: track 0.00 -> 41.8 mm, vias 0 -> 2
- net SERVO2: track 0.00 -> 38.7 mm, vias 0 -> 2
- net SERVO3: track 0.00 -> 34.7 mm, vias 0 -> 2
- net RELAY2: track 0.00 -> 34.1 mm, vias 0 -> 2
- net SERVO1: track 0.00 -> 31.2 mm, vias 0 -> 2
- net ADC2: track 0.00 -> 29.9 mm, vias 0 -> 2
- net RELAY1: track 0.00 -> 26.5 mm, vias 0 -> 2
- net ADC1: track 0.00 -> 25.3 mm, vias 0 -> 2
- net BOOT: track 0.00 -> 23.1 mm, vias 0 -> 1
- net +3.3V: track 0.00 -> 22.0 mm, vias 0 -> 23
- net OBLEDS: track 0.00 -> 13.8 mm, vias 0 -> 2
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- added copper zone on F.Cu, net +3.3V
- added copper zone on F.Cu, net +5V
- added copper zone on F.Cu, net LDO_V33
- added copper zone on F.Cu, net LINE_5V
- added copper zone on F.Cu, net LINE_V33
- added copper zone on F.Cu, net USB_5V
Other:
- board text removed: "x 4"

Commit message: Change schematic name
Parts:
- removed kibuzzard-68645E60: G***, kibuzzard-68645E60
- removed kibuzzard-68645E77: G***, kibuzzard-68645E77
- removed kibuzzard-68927F31: G***, kibuzzard-68927F31
- removed kibuzzard-68937D96: G***, kibuzzard-68937D96
- removed kibuzzard-68953BE7: G***, kibuzzard-68953BE7
- removed kibuzzard-68953C01: G***, kibuzzard-68953C01
- removed kibuzzard-68953F1F: G***, kibuzzard-68953F1F
- removed kibuzzard-68953F32: G***, kibuzzard-68953F32
- added C10: 0.1uF, Capacitor_SMD:C_0603_1608Metric, F.Cu at (91.7, 99.8)
- added C11: 0.1uF, Capacitor_SMD:C_0603_1608Metric, F.Cu at (87.1, 107.6)
- added C12: 1uF, Capacitor_SMD:C_0603_1608Metric, F.Cu at (89.0, 101.9)
- added C13: 0.1uF, Capacitor_SMD:C_0603_1608Metric, F.Cu at (87.6, 85.5)
- added C14: 0.1uF, Capacitor_SMD:C_0603_1608Metric, F.Cu at (91.0, 85.5)
- added C15: 0.1uF, Capacitor_SMD:C_0603_1608Metric, F.Cu at (94.3, 85.5)
- added C16: 0.1uF, Capacitor_SMD:C_0603_1608Metric, F.Cu at (97.7, 85.5)
- added C9: 1uF, Capacitor_SMD:C_0603_1608Metric, F.Cu at (91.5, 104.8)
- added R6: 4R7, Resistor_SMD:R_0603_1608Metric, F.Cu at (86.5, 102.8)
- added U8: SGP40-D-R4, CRG Makes:SON80P244X244X95-7N, F.Cu at (89.0, 104.0)
- added kibuzzard-689A6C29: G***, kibuzzard-689A6C29, B.Cu at (91.8, 88.0)
- added kibuzzard-689A6C42: G***, kibuzzard-689A6C42, B.Cu at (53.5, 95.8)
- added kibuzzard-689A6D37: G***, kibuzzard-689A6D37, F.Cu at (90.2, 88.8)
- added kibuzzard-689A6D3F: G***, kibuzzard-689A6D3F, F.Cu at (90.2, 94.8)
- added kibuzzard-689A71A2: G***, kibuzzard-689A71A2, B.Cu at (78.8, 76.4)
- added kibuzzard-689A71E4: G***, kibuzzard-689A71E4, F.Cu at (62.0, 103.9)
- added kibuzzard-689A9524: G***, kibuzzard-689A9524, F.Cu at (90.8, 107.5)
- added kibuzzard-689A9DAD: G***, kibuzzard-689A9DAD, F.Cu at (94.0, 101.8)
- added kibuzzard-689A9DC1: G***, kibuzzard-689A9DC1, F.Cu at (94.5, 99.7)
- D1, D2, D3, D4: footprint LED_SMD:LED_WS2812B-2020_PLCC4_2.0x2.0mm -> CRGM Passive:LED_WS2812B-2020_PLCC4_2.0x2.0mm
- moved kibuzzard-68953DED 12.1 mm to (97.1, 81.3)
- moved U2 3.44 mm to (89.0, 99.0)
- moved D1 3.23 mm to (87.8, 83.3), turned to 180 degrees
- moved D2 2.43 mm to (91.1, 83.3), turned to 180 degrees
- moved kibuzzard-68953ED1 2.06 mm to (68.2, 103.7)
- moved kibuzzard-68953ED8 2.06 mm to (68.0, 108.3)
- moved kibuzzard-68953EC7 1.83 mm to (68.2, 99.2)
- moved kibuzzard-68953DE5 1.70 mm to (89.4, 81.3)
- moved D3 1.67 mm to (94.5, 83.3), turned to 180 degrees
- moved LOGO3 1.60 mm to (78.8, 74.5)
- moved kibuzzard-68953EE0 1.59 mm to (83.8, 105.2)
- moved kibuzzard-68953EEB 1.59 mm to (83.8, 100.8)
- moved LOGO1 1.53 mm to (92.7, 76.5)
- moved J5 1.50 mm to (95.0, 90.0)
- moved J6 1.50 mm to (95.0, 96.0)
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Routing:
- net +3.3V: track 22.0 -> 36.0 mm, vias 23 -> 25
- net SDA: track 46.9 -> 57.2 mm, vias 4 -> 5
- net SCL: track 49.0 -> 55.1 mm, vias 4 -> 6
- net GND: track 42.6 -> 47.4 mm, vias 39 -> 40
- net Net-(U8-VDD): track 0.00 -> 3.35 mm
- net Net-(D1-DOUT): track 4.38 -> 1.98 mm
- net Net-(D3-DOUT): track 4.38 -> 1.98 mm
- net Net-(D2-DOUT): track 4.37 -> 1.98 mm
- net OBLEDS: track 13.8 -> 11.6 mm
- net ADC2: track 29.9 -> 31.0 mm
- net ADC1: track 25.3 -> 26.4 mm
- net EN: track 41.8 -> 42.5 mm
- net BOOT: track 23.1 -> 22.5 mm
